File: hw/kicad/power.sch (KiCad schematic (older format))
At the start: 60 parts, among them Q1 FDBL0110N60, Q2 FDBL0110N60, Q3 FDBL0110N60, Q4 FDBL0110N60, Q5 FDBL0110N60, Q6 FDBL0110N60, U2 LM5101A, U3 LM5101A, U4 LM5101A, U5 INA240A2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

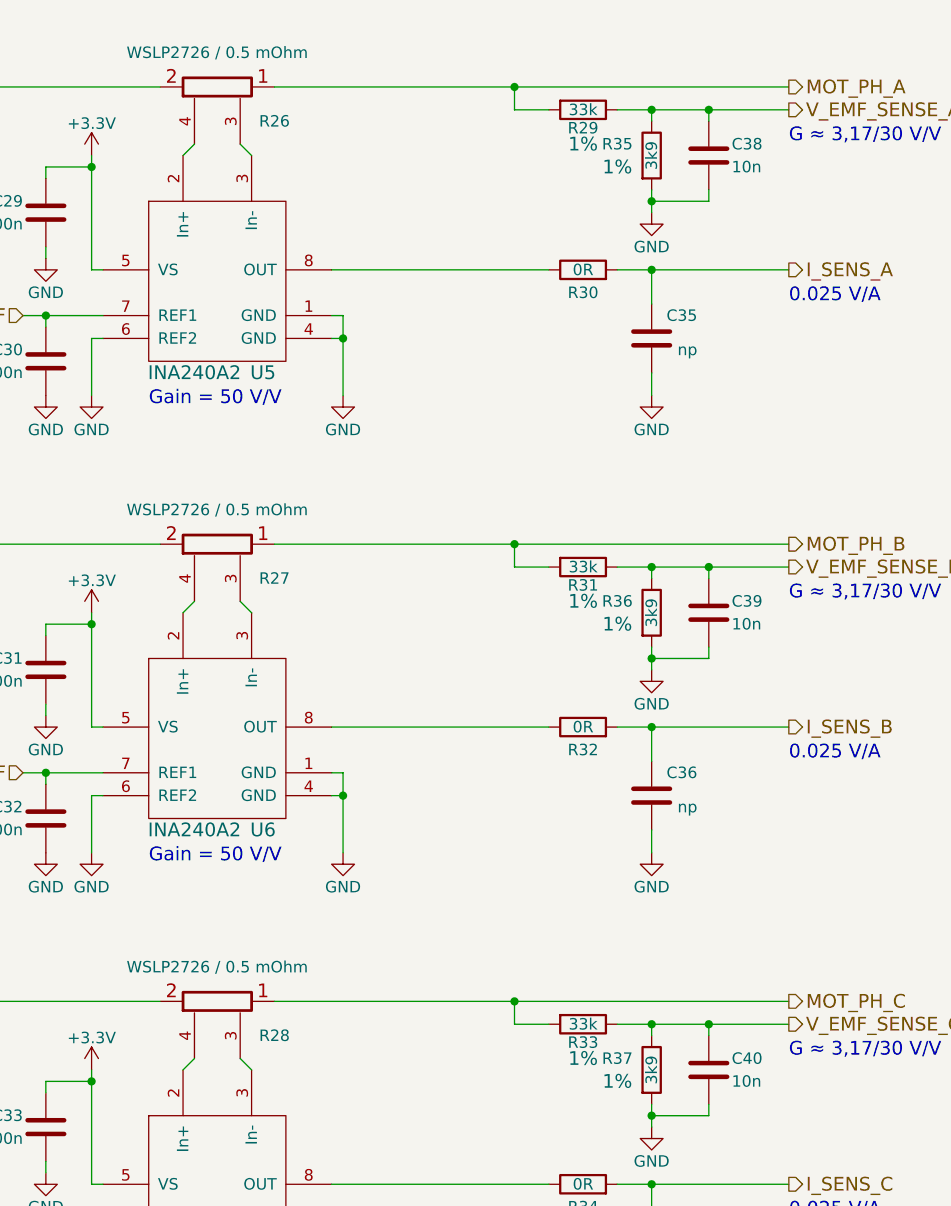
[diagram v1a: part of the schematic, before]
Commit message: Alternative layout with smaller total vertical footprint
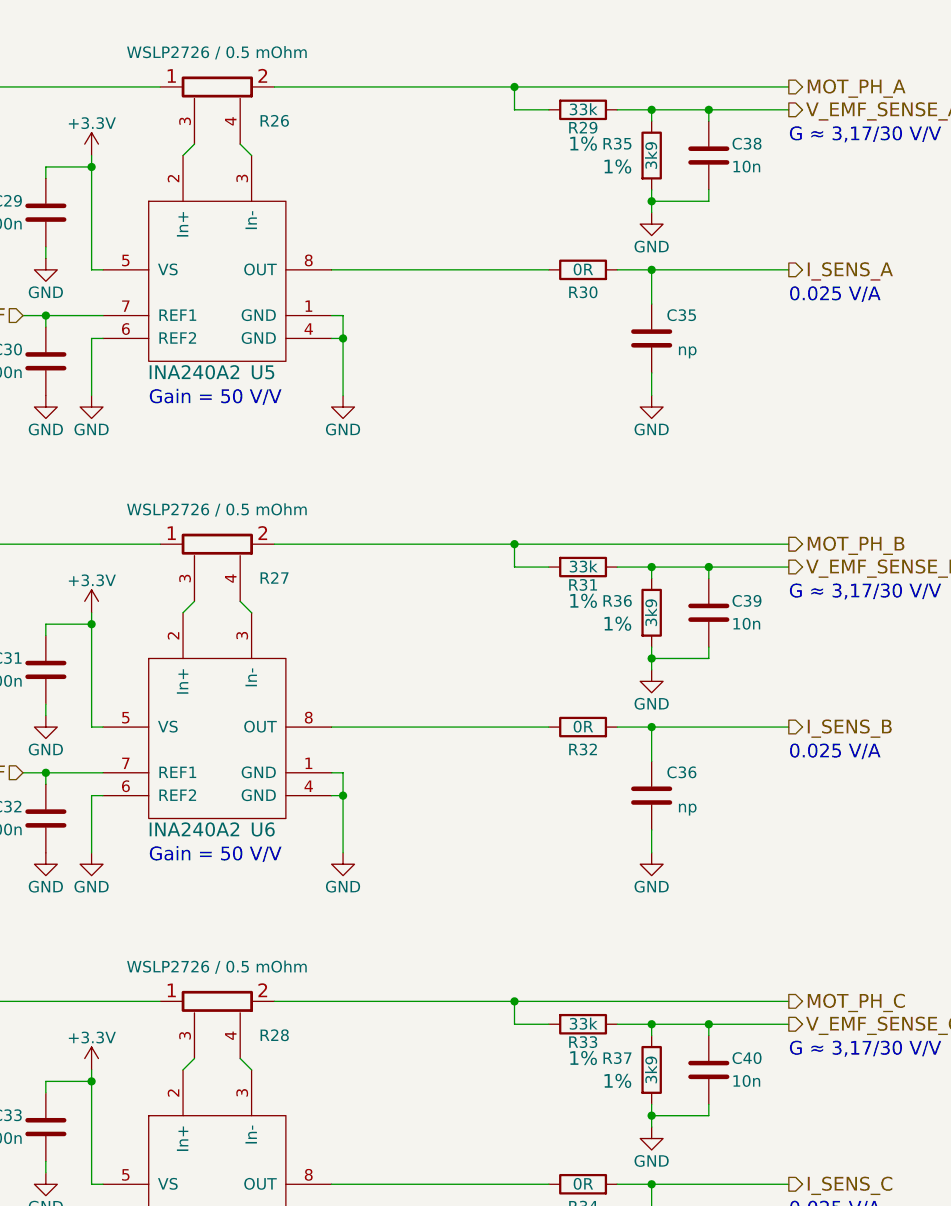
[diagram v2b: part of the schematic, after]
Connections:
- net MOT_PH_A: now also R26.2; no longer R26.1
- net MOT_PH_B: now also R27.2; no longer R27.1
- net MOT_PH_C: now also R28.2; no longer R28.1
- net at C24.1, Q1.2 (S), Q2.3 (D)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: now also R26.1; no longer R26.2
- net at R26.3: now also U5.2 (In+); no longer U5.3 (In-)
- net at R26.4: now also U5.3 (In-); no longer U5.2 (In+)
- net at C25.1, Q3.2 (S), Q4.3 (D)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: now also R27.1; no longer R27.2
- net at R27.3: now also U6.2 (In+); no longer U6.3 (In-)
- net at R27.4: now also U6.3 (In-); no longer U6.2 (In+)
- net at C26.1, Q5.2 (S), Q6.3 (D)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: now also R28.1; no longer R28.2
- net at R28.3: now also U7.2 (In+); no longer U7.3 (In-)
- net at R28.4: now also U7.3 (In-); no longer U7.2 (In+)
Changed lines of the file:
@@
 AR Path="/581DC4BA" Ref="R26"  Part="1"
 AR Path="/58153909/581DC4BA" Ref="R26"  Part="1"
-F 0 "R26" V 7100 550 50  0000 C CNN
+F 0 "R26" V 7100 1050 50  0000 C CNN
 F 1 "WSLP2726 / 0.5 mOhm" V 7400 800 50  0000 C CNN
 F 2 "WSLP2726:WSLP2726" H 7250 800 60  0001 C CNN
 F 3 "" H 7250 800 60  0000 C CNN
 	1    7250 800
-	0    -1   -1   0
+	0    1    -1   0
 $EndComp
 $Comp
@@
 AR Path="/5827256F" Ref="R27"  Part="1"
 AR Path="/58153909/5827256F" Ref="R27"  Part="1"
-F 0 "R27" V 7100 2550 50  0000 C CNN
+F 0 "R27" V 7100 3050 50  0000 C CNN
 F 1 "WSLP2726 / 0.5 mOhm" V 7400 2800 50  0000 C CNN
 F 2 "WSLP2726:WSLP2726" H 7250 2800 60  0001 C CNN
 F 3 "" H 7250 2800 60  0000 C CNN
 	1    7250 2800
-	0    -1   -1   0
+	0    1    -1   0
 $EndComp
 Text HLabel 9750 2800 2    60   Output ~ 0
@@
 AR Path="/5827284D" Ref="R28"  Part="1"
 AR Path="/58153909/5827284D" Ref="R28"  Part="1"
-F 0 "R28" V 7100 4550 50  0000 C CNN
+F 0 "R28" V 7100 5050 50  0000 C CNN
 F 1 "WSLP2726 / 0.5 mOhm" V 7400 4800 50  0000 C CNN
 F 2 "WSLP2726:WSLP2726" H 7250 4800 60  0001 C CNN
 F 3 "" H 7250 4800 60  0000 C CNN
 	1    7250 4800
-	0    -1   -1   0
+	0    1    -1   0
 $EndComp
 Text HLabel 9750 4800 2    60   Output ~ 0
@@
 	5350 2800 7000 2800
 Wire Wire Line
-	5350 800  7000 800
-Wire Wire Line
 	5350 4800 7000 4800
 Wire Wire Line
-	9750 800  7500 800
+	7500 800  9750 800
 Wire Wire Line
 	8700 900  8550 900
@@
 Connection ~ 8550 2800
 Wire Wire Line
-	9750 4800 7500 4800
+	7500 4800 9750 4800
 Wire Wire Line
 	8700 4900 8550 4900
@@
 G ≈ 3,17/30 V/V
 Wire Wire Line
+	5350 800  7000 800
+Wire Wire Line
 	7100 1100 7150 1050

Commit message: work
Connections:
- net PH_A: now reaches C24.1, Q1.2 (S), Q2.3 (D), R20.2, R26.1, U2.4 (HS)
- net PH_B: now reaches C25.1, Q3.2 (S), Q4.3 (D), R22.2, R27.1, U3.4 (HS)
- net PH_C: now reaches C26.1, Q5.2 (S), Q6.3 (D), R24.2, R28.1, U4.4 (HS)
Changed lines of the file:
@@
 Wire Wire Line
 	7350 1050 7400 1100
+Text Label 4250 1600 0    60   ~ 0
+PH_A
+Text Label 4250 4100 0    60   ~ 0
+PH_B
+Text Label 4250 6600 0    60   ~ 0
+PH_C
+Text Label 9750 800  2    60   ~ 0
+MOT_PH_A
+Text Label 9750 2800 2    60   ~ 0
+MOT_PH_B
+Text Label 9750 4800 2    60   ~ 0
+MOT_PH_C
+Text Label 9750 1600 2    60   ~ 0
+I_SENSE_A
+Text Label 9750 3600 2    60   ~ 0
+I_SENSE_B
+Text Label 9750 5600 2    60   ~ 0
+I_SENSE_C
+Text Label 9750 900  2    60   ~ 0
+V_EMF_SENSE_A
+Text Label 9750 2900 2    60   ~ 0
+V_EMF_SENSE_B
+Text Label 9750 4900 2    60   ~ 0
+V_EMF_SENSE_C
 $EndSCHEMATC

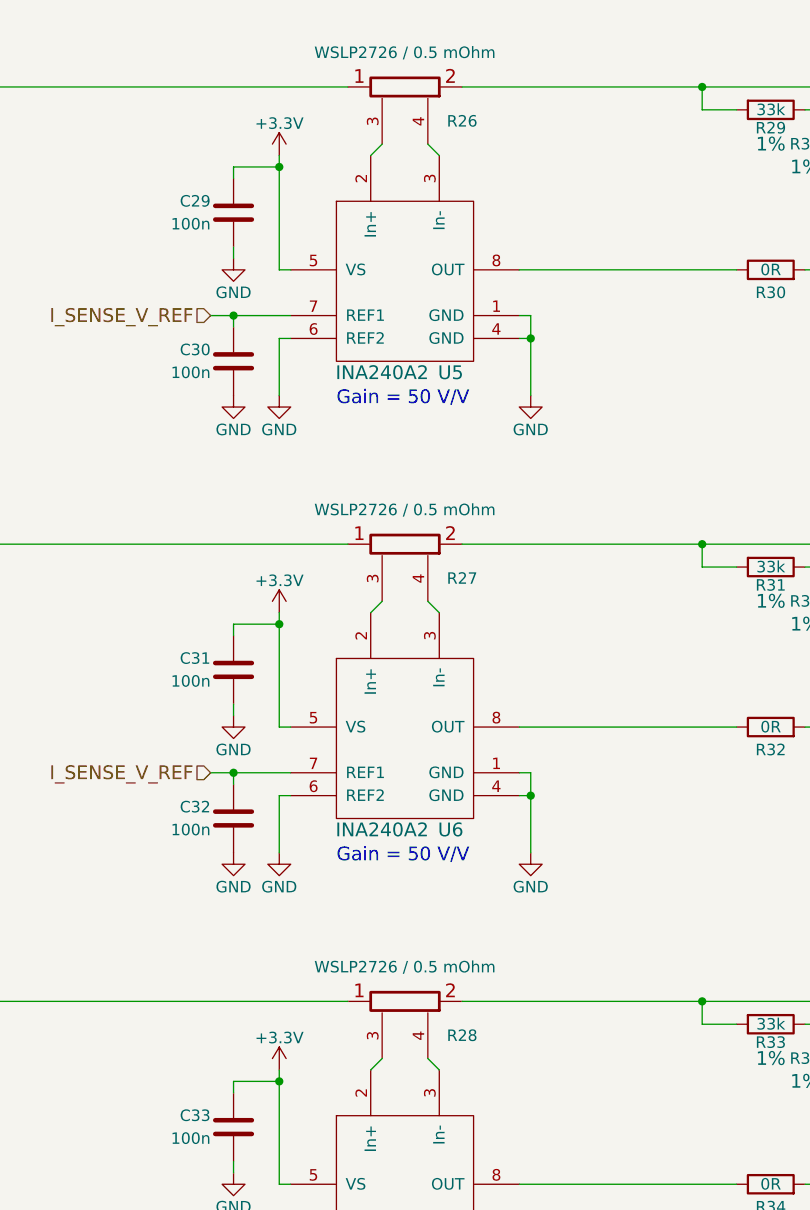
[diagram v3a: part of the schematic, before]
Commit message: Aligned, started rework current shunt layout and copper pour
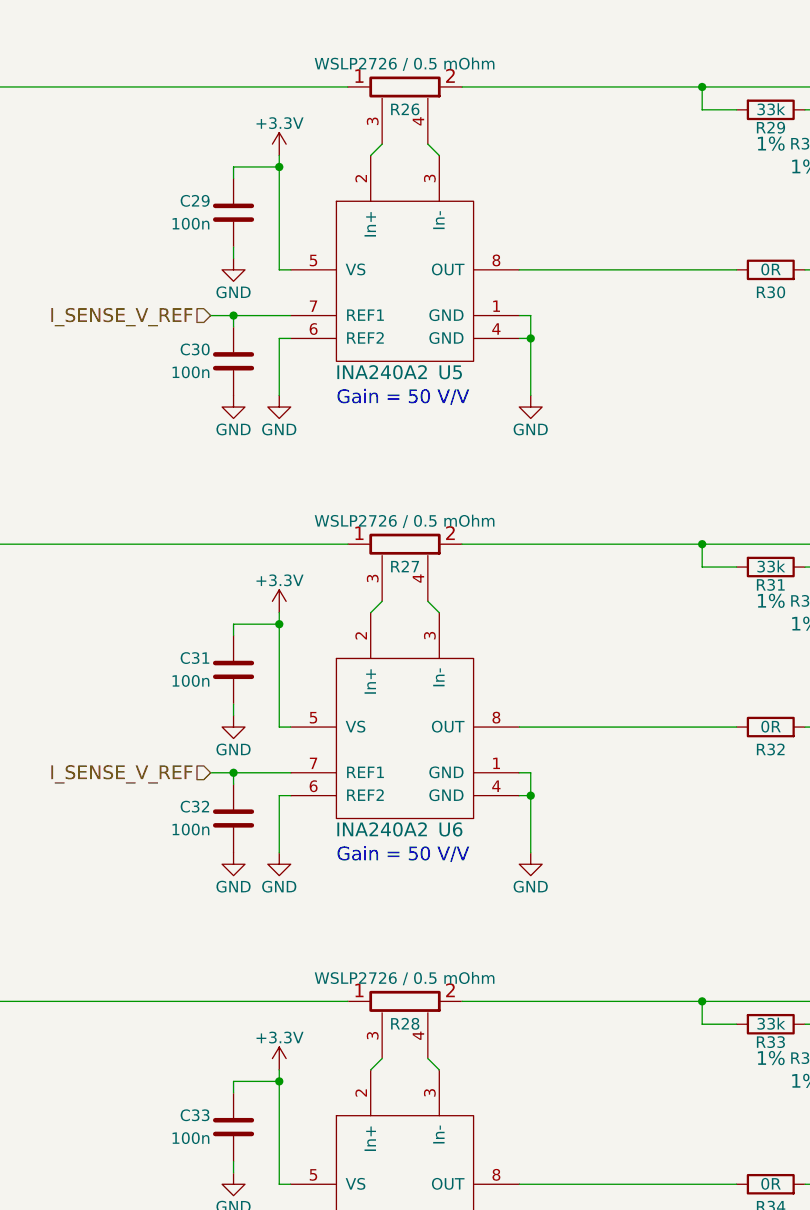
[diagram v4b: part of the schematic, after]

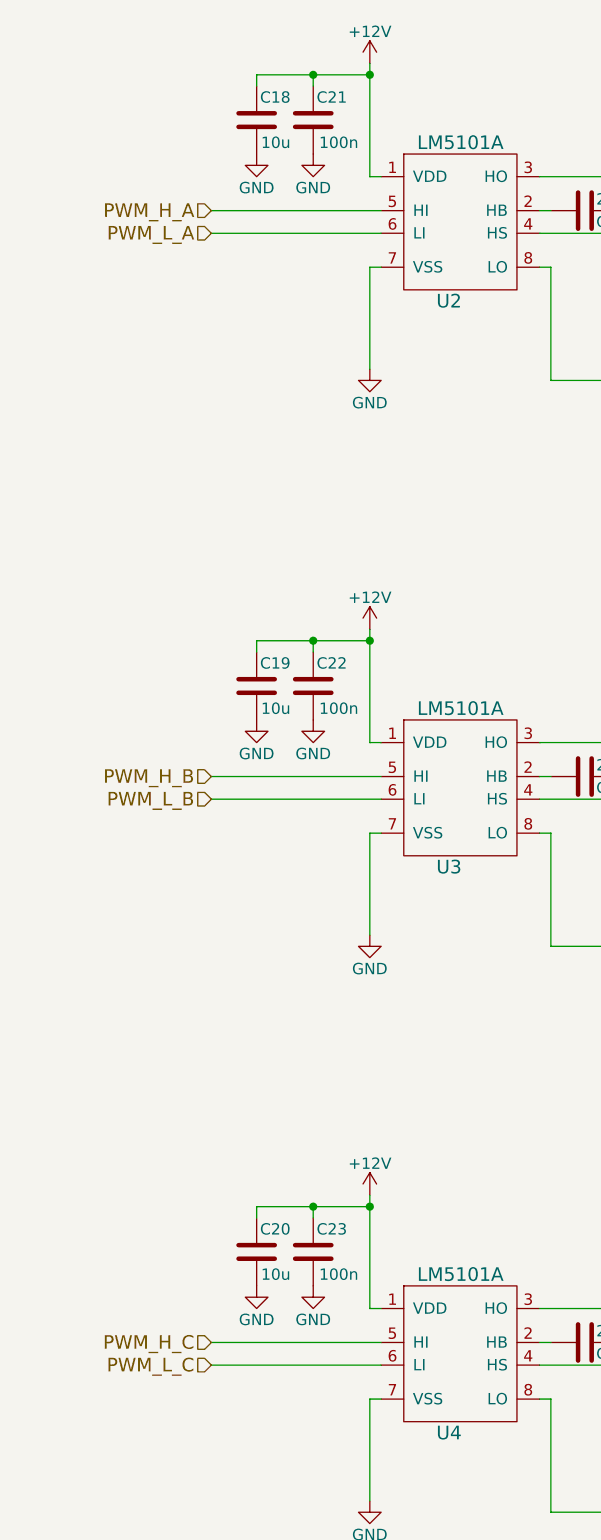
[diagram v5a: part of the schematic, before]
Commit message: Add test pads
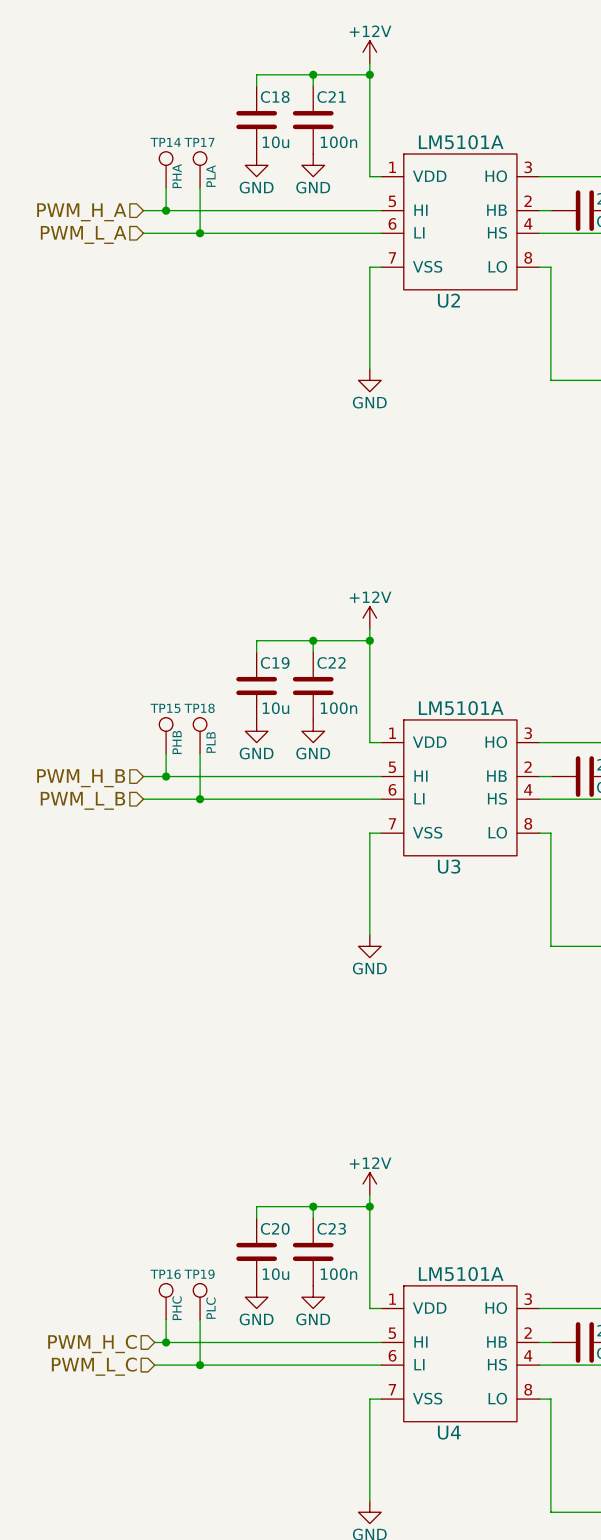
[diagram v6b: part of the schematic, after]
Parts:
- added TP14: PHA, Measurement_Points:Measurement_Point_Round-SMD-Pad_Small, symbol TESTPAD
- added TP15: PHB, Measurement_Points:Measurement_Point_Round-SMD-Pad_Small, symbol TESTPAD
- added TP16: PHC, Measurement_Points:Measurement_Point_Round-SMD-Pad_Small, symbol TESTPAD
- added TP17: PLA, Measurement_Points:Measurement_Point_Round-SMD-Pad_Small, symbol TESTPAD
- added TP18: PLB, Measurement_Points:Measurement_Point_Round-SMD-Pad_Small, symbol TESTPAD
- added TP19: PLC, Measurement_Points:Measurement_Point_Round-SMD-Pad_Small, symbol TESTPAD
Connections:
- net PWM_H_A: now also TP14.1
- net PWM_H_B: now also TP15.1
- net PWM_H_C: now also TP16.1
- net PWM_L_A: now also TP17.1
- net PWM_L_B: now also TP18.1
- net PWM_L_C: now also TP19.1

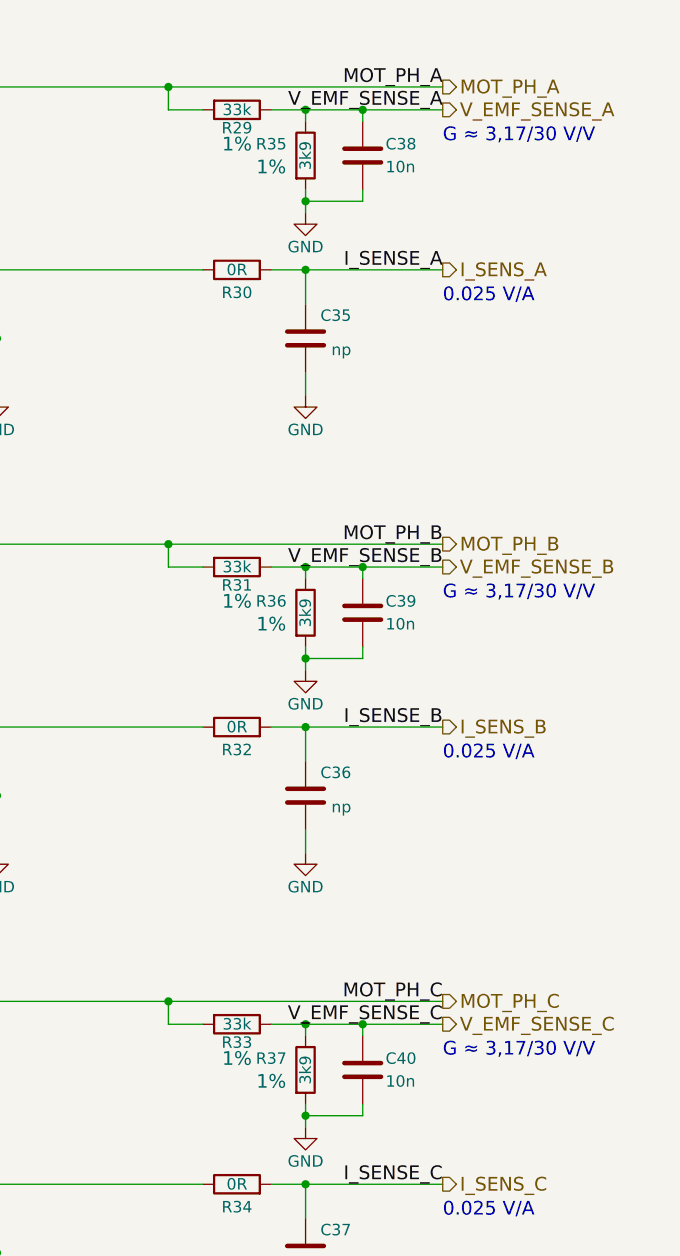
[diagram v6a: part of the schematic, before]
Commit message: HW: Changed rc-filter capacitor to increase BEMF-sense bandwidth.
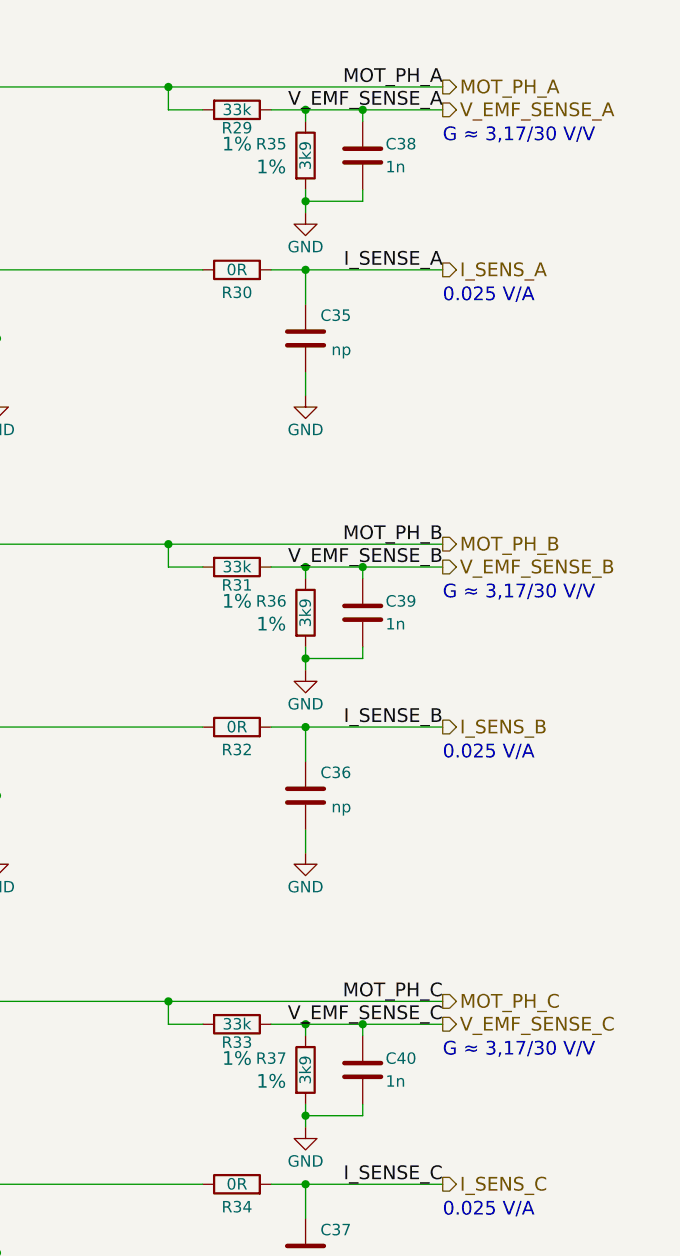
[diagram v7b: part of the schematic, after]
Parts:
- C38, C39, C40: value 10n -> 1n
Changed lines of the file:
@@
 P 9400 1100
 F 0 "C38" H 9500 1150 50  0000 L CNN
-F 1 "10n" H 9500 1050 50  0000 L CNN
+F 1 "1n" H 9500 1050 50  0000 L CNN
 F 2 "Capacitors_SMD:C_0402" H 9438 950 30  0001 C CNN
 F 3 "" H 9400 1100 60  0000 C CNN
@@
 P 9400 3100
 F 0 "C39" H 9500 3150 50  0000 L CNN
-F 1 "10n" H 9500 3050 50  0000 L CNN
+F 1 "1n" H 9500 3050 50  0000 L CNN
 F 2 "Capacitors_SMD:C_0402" H 9438 2950 30  0001 C CNN
 F 3 "" H 9400 3100 60  0000 C CNN
@@
 P 9400 5100
 F 0 "C40" H 9500 5150 50  0000 L CNN
-F 1 "10n" H 9500 5050 50  0000 L CNN
+F 1 "1n" H 9500 5050 50  0000 L CNN
 F 2 "Capacitors_SMD:C_0402" H 9438 4950 30  0001 C CNN
 F 3 "" H 9400 5100 60  0000 C CNN
